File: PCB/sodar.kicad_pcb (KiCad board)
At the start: 2 copper layers, 70 parts, among them J1 Screw_Terminal_01x02, J2 Conn_02x12_Counter_Clockwise, J3 Conn_01x02, U1 TC78H621FNG, U10 TC78H621FNG, U2 TC78H621FNG, U3 TC78H621FNG, U4 TC78H621FNG, U5 TC78H621FNG, U6 TC78H621FNG, U7 TC78H621FNG, U8 TC78H621FNG, U9 TC78H621FNG

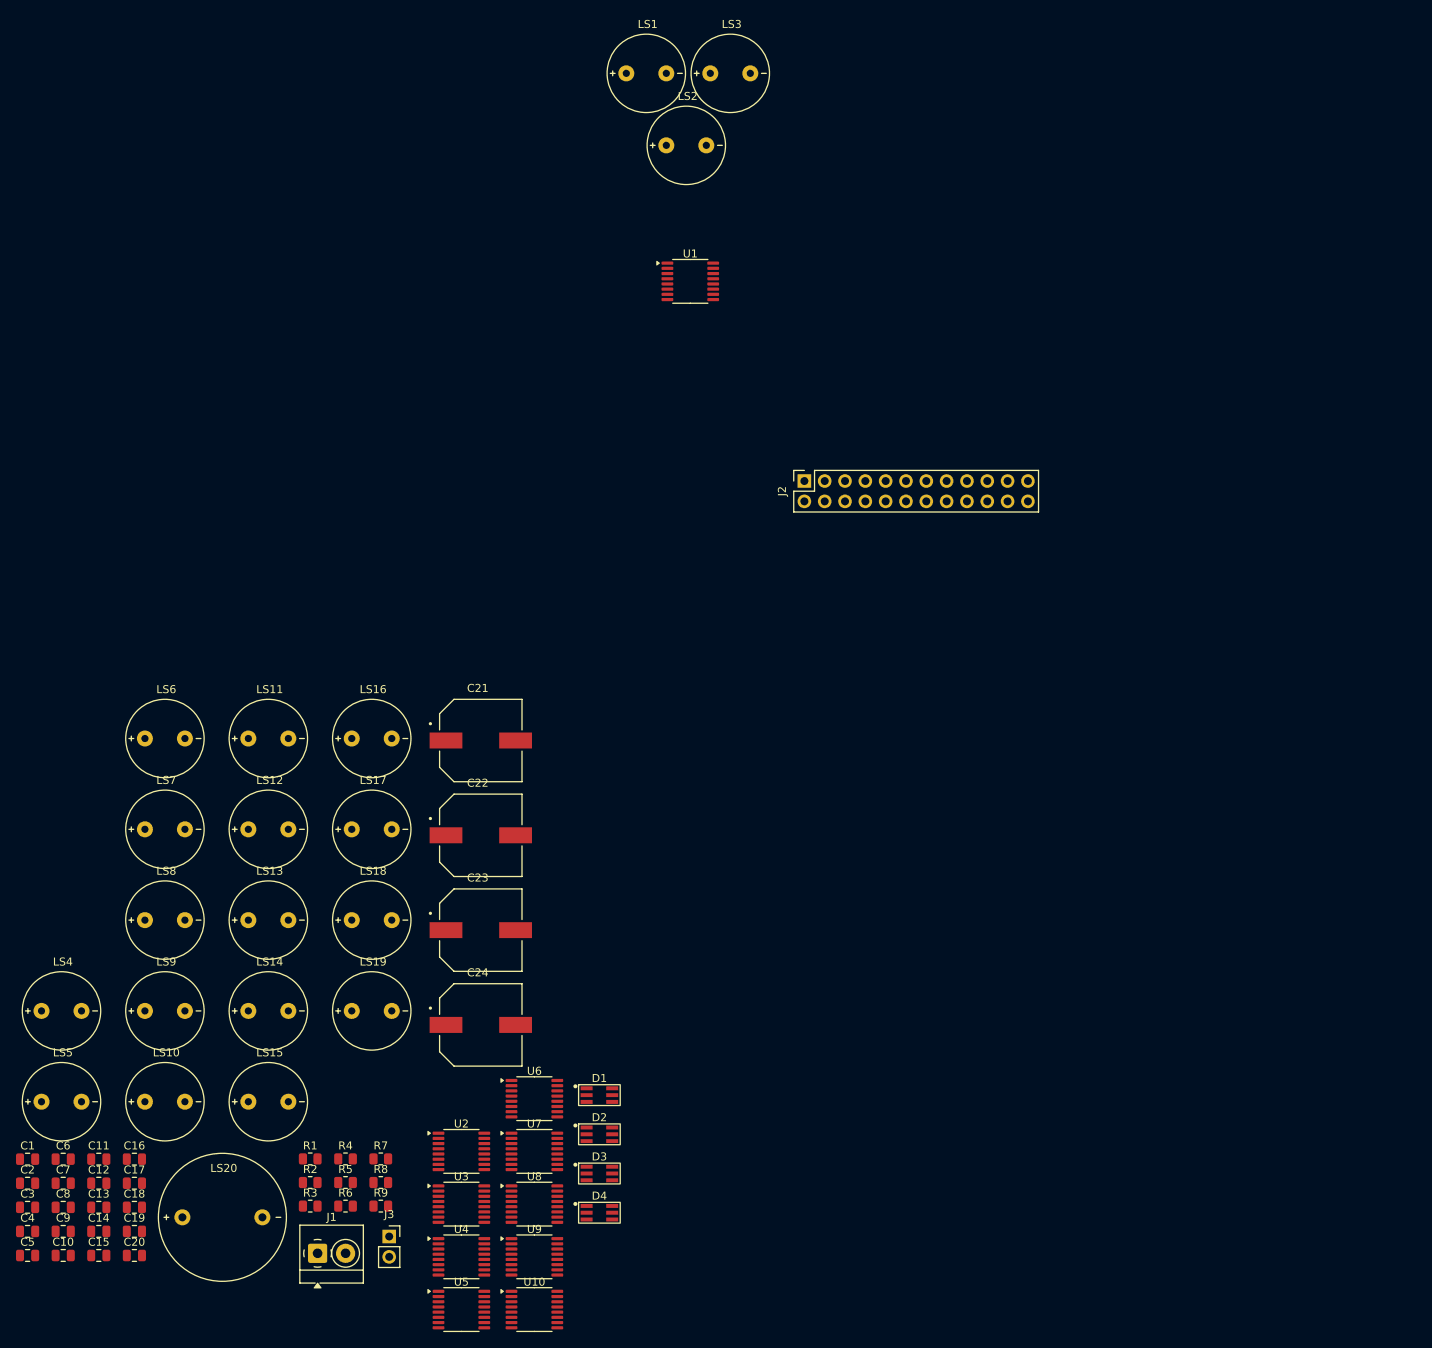
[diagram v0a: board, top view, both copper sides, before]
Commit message: Moved the transducers and the drivers in the right positions
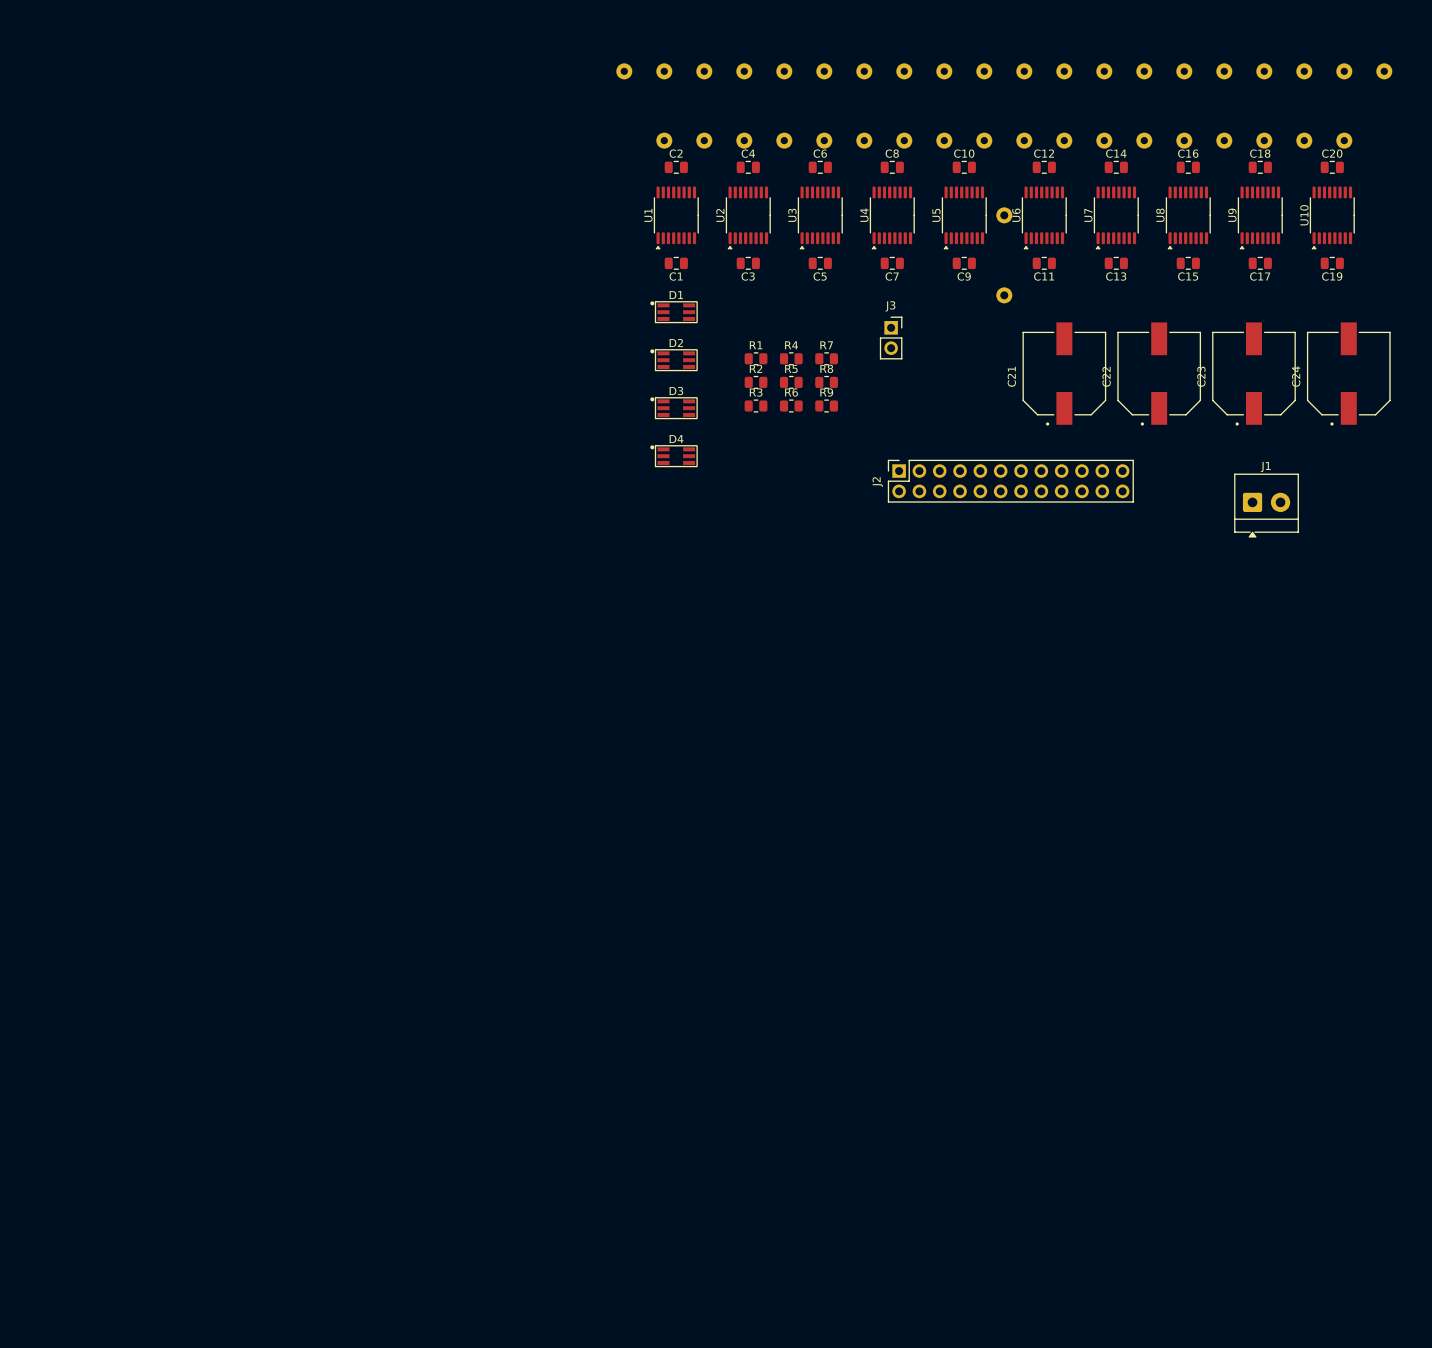
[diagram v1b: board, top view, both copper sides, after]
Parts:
- LS1, LS10, LS11, LS12, LS13, LS14, LS15, LS16, LS17, LS18, LS19, LS2, LS20, LS3, LS4, LS5, LS6, LS7, LS8, LS9: moved to B.Cu
- moved C20 202.3 mm to (191.0, 47.0)
- moved C19 192.5 mm to (191.0, 59.0), turned to 180 degrees
- moved C18 191.6 mm to (182.0, 47.0)
- moved C15 184.2 mm to (173.0, 59.0), turned to 180 degrees
- moved C14 184.0 mm to (164.0, 47.0)
- moved C17 181.7 mm to (182.0, 59.0), turned to 180 degrees
- moved C16 180.9 mm to (173.0, 47.0)
- moved C10 176.6 mm to (145.0, 47.0)
- moved LS15 174.0 mm to (175.0, 35.0)
- moved C13 173.5 mm to (164.0, 59.0), turned to 180 degrees
- moved C12 173.5 mm to (155.0, 47.0)
- moved LS19 170.8 mm to (195.0, 35.0)
- moved U10 169.3 mm to (191.0, 53.0), turned to 90 degrees
- moved C8 166.3 mm to (136.0, 47.0)
- moved C9 165.3 mm to (145.0, 59.0), turned to 180 degrees
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
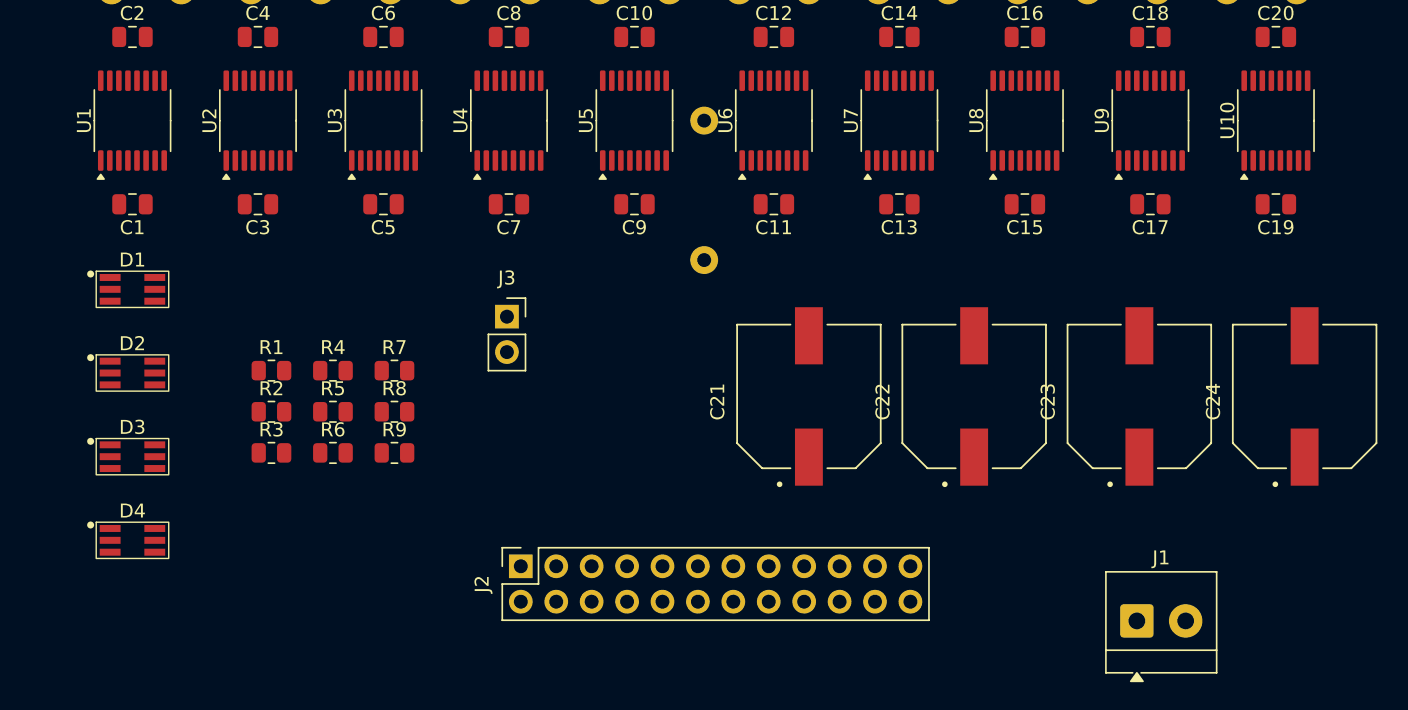
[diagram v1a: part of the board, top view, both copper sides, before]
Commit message: first PCB layout finished, to be reviewed
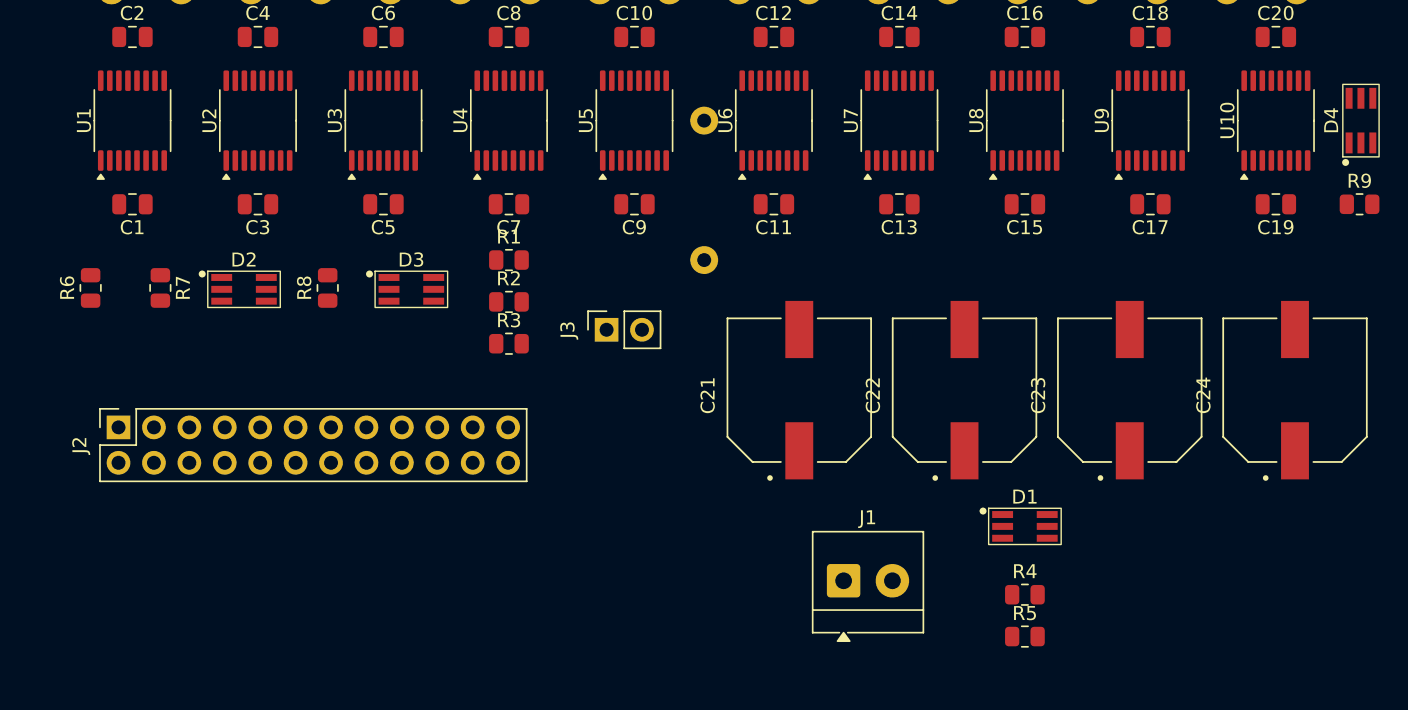
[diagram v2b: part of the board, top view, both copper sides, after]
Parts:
- moved D4 90.4 mm to (195.0, 53.0), turned to 90 degrees
- moved R9 71.5 mm to (197.0, 59.0)
- moved D1 66.2 mm to (173.0, 80.0)
- moved R5 52.2 mm to (173.0, 90.0)
- moved R4 52.2 mm to (173.0, 87.0)
- moved J2 30.5 mm to (108.0, 75.0)
- moved D3 23.3 mm to (129.0, 63.0)
- moved J1 21.2 mm to (160.0, 86.0)
- moved R6 21.0 mm to (106.0, 65.0), turned to 90 degrees
- moved R1 18.8 mm to (136.0, 63.0)
- moved R2 18.8 mm to (136.0, 66.0)
- moved R3 18.7 mm to (136.0, 69.0)
- moved R7 17.8 mm to (111.0, 65.0), turned to -90 degrees
- moved R8 10.1 mm to (123.0, 65.0), turned to 90 degrees
- moved D2 10.0 mm to (117.0, 63.0)
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
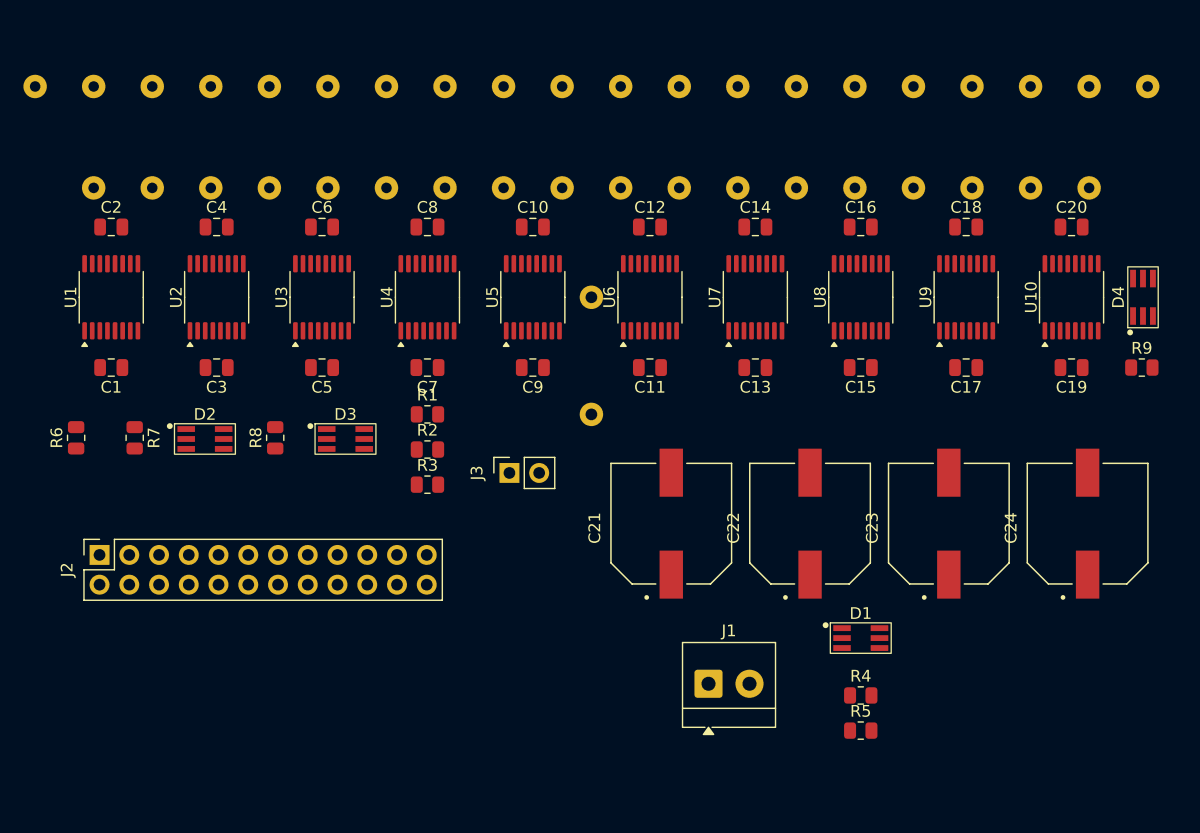
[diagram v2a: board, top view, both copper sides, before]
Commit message: My idea of designe with placement change and begin of connections
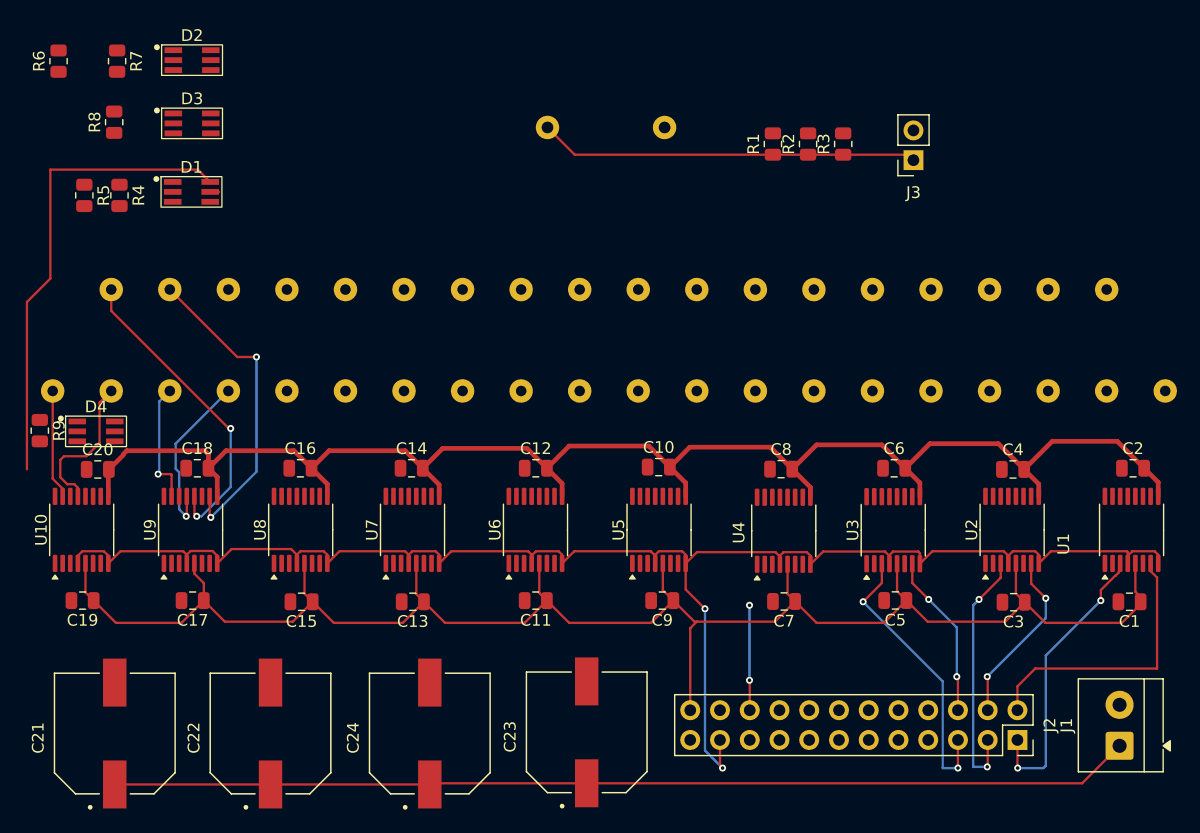
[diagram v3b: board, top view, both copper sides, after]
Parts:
- moved LS1 95.1 mm to (196.5, 61.0)
- moved R9 94.3 mm to (102.9, 64.4), turned to -90 degrees
- moved LS19 92.2 mm to (106.5, 61.0)
- moved C2 89.6 mm to (196.2, 67.6)
- moved U1 89.4 mm to (196.1, 72.9)
- moved C1 89.2 mm to (195.9, 79.0)
- moved D4 87.8 mm to (107.7, 62.4), turned to 0 degrees
- moved U10 86.8 mm to (106.5, 72.9)
- moved C19 86.8 mm to (106.5, 78.9)
- moved C20 85.7 mm to (107.8, 67.7)
- moved LS2 82.0 mm to (191.5, 52.3)
- moved R5 80.5 mm to (106.7, 44.3), turned to -90 degrees
- moved J2 80.0 mm to (186.4, 90.8), turned to -90 degrees
- moved LS18 79.0 mm to (111.5, 52.3)
- moved R4 76.4 mm to (109.7, 44.3), turned to -90 degrees
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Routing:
- net Vdrive: track 0.00 -> 218.5 mm
- net +3V3: track 0.00 -> 148.0 mm
- net EN: track 0.00 -> 139.7 mm, vias 0 -> 2
- net STBY: track 0.00 -> 49.5 mm, vias 0 -> 2
- net RX: track 0.00 -> 32.4 mm
- net Net-(U9-BO2): track 0.00 -> 26.9 mm, vias 0 -> 2
- net Net-(U9-BO1): track 0.00 -> 26.9 mm, vias 0 -> 2
- net S1: track 0.00 -> 24.8 mm, vias 0 -> 2
- net S5: track 0.00 -> 24.6 mm, vias 0 -> 2
- net S2: track 0.00 -> 23.8 mm
- net S3: track 0.00 -> 21.9 mm, vias 0 -> 2
- net S4: track 0.00 -> 15.1 mm, vias 0 -> 2
- net Net-(U9-AO2): track 0.00 -> 14.7 mm, vias 0 -> 1
- net S6: track 0.00 -> 14.1 mm, vias 0 -> 2
- net Net-(U10-AO2): track 0.00 -> 13.1 mm
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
